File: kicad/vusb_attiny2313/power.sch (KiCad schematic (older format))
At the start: 10 parts, among them U6 LT1073CS

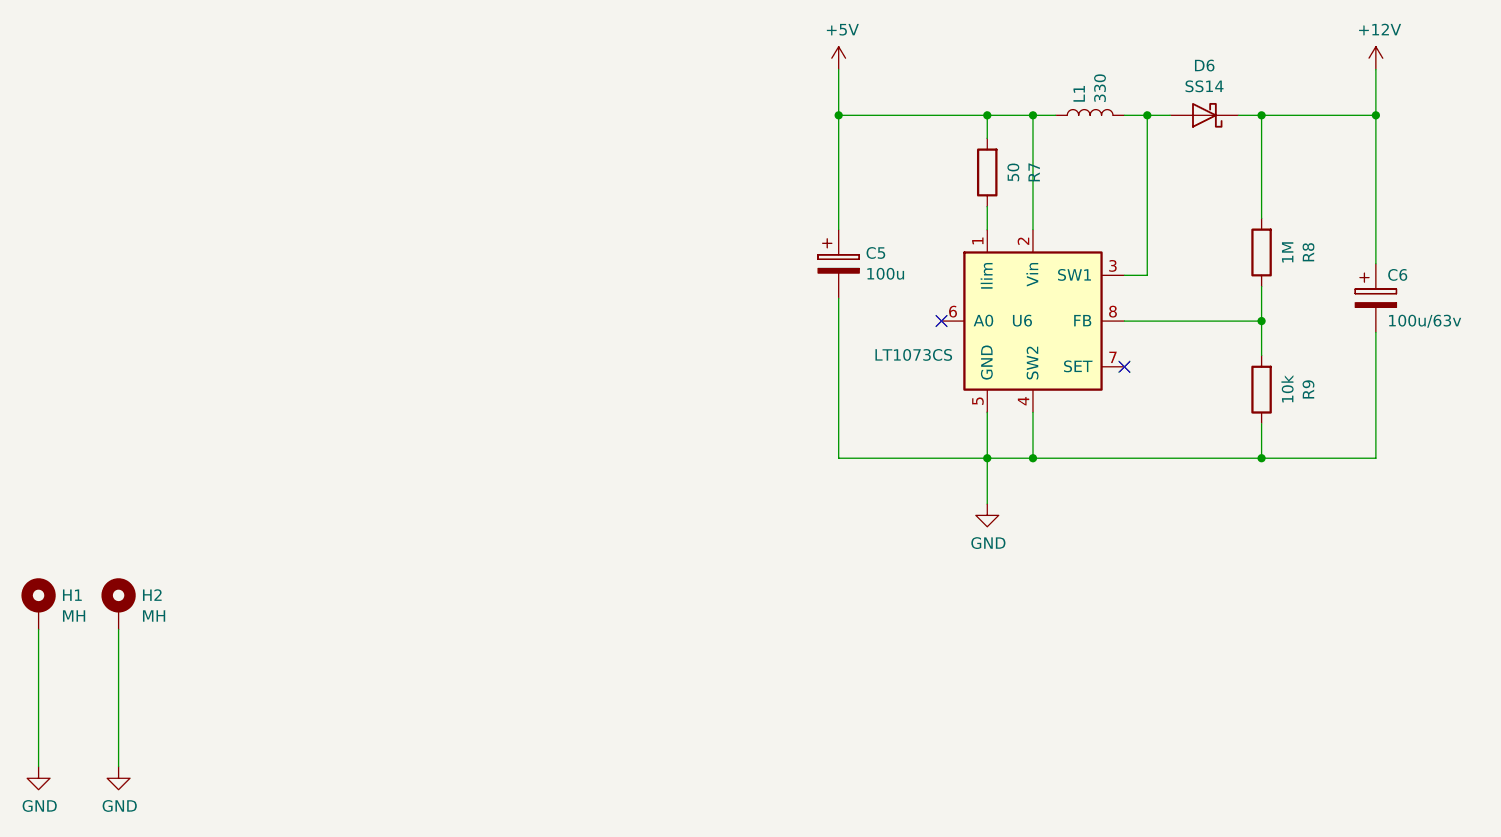
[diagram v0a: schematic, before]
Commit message: fuses angepasst!
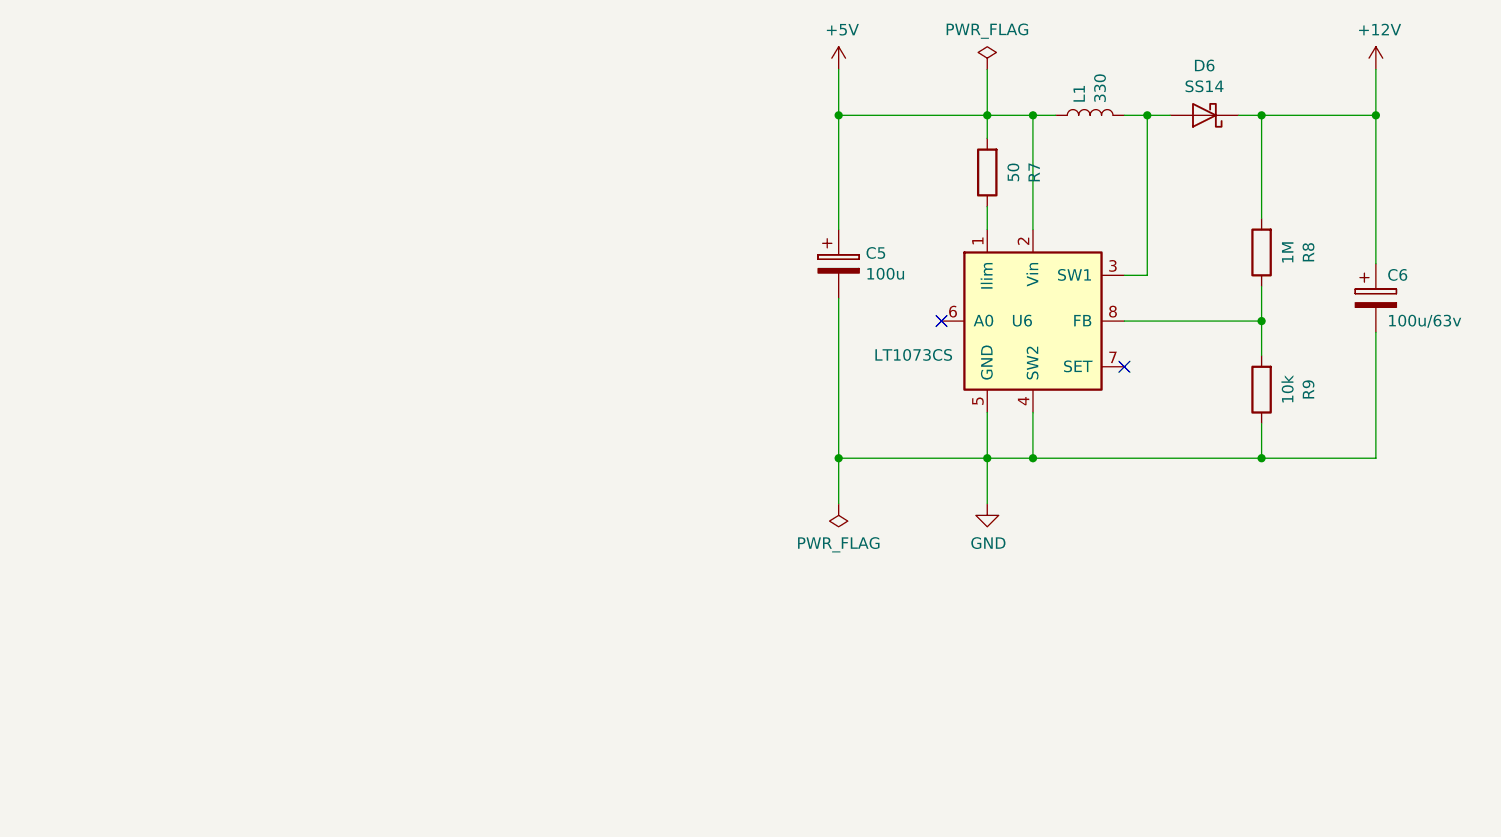
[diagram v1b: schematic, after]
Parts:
- removed H1, H2: MH, MountingHole:MountingHole_3.2mm_M3_DIN965_Pad, symbol Mechanical:MountingHole_Pad
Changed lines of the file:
@@
 $Descr A4 11693 8268
 encoding utf-8
-Sheet 2 2
+Sheet 2 3
 Title ""
 Date ""
@@
 	1    0    0    -1
 $EndComp
-Wire Wire Line
-	1300 4750 1300 5350
-Wire Wire Line
-	950  4750 950  5350
-$Comp
-L Mechanical:MountingHole_Pad H2
-U 1 1 5C571FCD
-P 1300 4650
-F 0 "H2" H 1400 4699 50  0000 L CNN
-F 1 "MH" H 1400 4608 50  0000 L CNN
-F 2 "MountingHole:MountingHole_3.2mm_M3_DIN965_Pad" H 1300 4650 50  0001 C CNN
-F 3 "~" H 1300 4650 50  0001 C CNN
-	1    1300 4650
-	1    0    0    -1
-$EndComp
-$Comp
-L Mechanical:MountingHole_Pad H1
-U 1 1 5C571652
-P 950 4650
-F 0 "H1" H 1050 4699 50  0000 L CNN
-F 1 "MH" H 1050 4608 50  0000 L CNN
-F 2 "MountingHole:MountingHole_3.2mm_M3_DIN965_Pad" H 950 4650 50  0001 C CNN
-F 3 "~" H 950 4650 50  0001 C CNN
-	1    950  4650
-	1    0    0    -1
-$EndComp
-$Comp
-L power:GND #PWR032
-U 1 1 5C15DD1A
-P 1300 5350
-F 0 "#PWR032" H 1300 5100 50  0001 C CNN
-F 1 "GND" H 1305 5177 50  0000 C CNN
-F 2 "" H 1300 5350 50  0001 C CNN
-F 3 "" H 1300 5350 50  0001 C CNN
-	1    1300 5350
-	1    0    0    -1
-$EndComp
-$Comp
-L power:GND #PWR031
-U 1 1 5C15D6F6
-P 950 5350
-F 0 "#PWR031" H 950 5100 50  0001 C CNN
-F 1 "GND" H 955 5177 50  0000 C CNN
-F 2 "" H 950 5350 50  0001 C CNN
-F 3 "" H 950 5350 50  0001 C CNN
-	1    950  5350
-	1    0    0    -1
-$EndComp
+$Comp
+L power:PWR_FLAG #FLG0102
+U 1 1 5D470A7F
+P 4450 4200
+F 0 "#FLG0102" H 4450 4275 50  0001 C CNN
+F 1 "PWR_FLAG" H 4450 4373 50  0000 C CNN
+F 2 "" H 4450 4200 50  0001 C CNN
+F 3 "~" H 4450 4200 50  0001 C CNN
+	1    4450 4200
+	-1   0    0    1
+$EndComp
+Wire Wire Line
+	4450 4200 4450 4000
+Connection ~ 4450 4000
+$Comp
+L power:PWR_FLAG #FLG0103
+U 1 1 5D470ED0
+P 5100 2300
+F 0 "#FLG0103" H 5100 2375 50  0001 C CNN
+F 1 "PWR_FLAG" H 5100 2474 50  0000 C CNN
+F 2 "" H 5100 2300 50  0001 C CNN
+F 3 "~" H 5100 2300 50  0001 C CNN
+	1    5100 2300
+	1    0    0    -1
+$EndComp
+Wire Wire Line
+	5100 2300 5100 2500
 $EndSCHEMATC
